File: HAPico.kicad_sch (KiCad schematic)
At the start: 30 parts, among them J1 GP 2, J2 GP 3, J3 GP 6, J4 GP 7, J5 GP10, J6 GP11, J7 GP20, J8 GP21, J9 Power Switch, Q1 IRLR024N, Q2 IRLR024N, Q3 IRLR024N, Q4 IRLR024N, Q5 IRLR024N, Q6 IRLR024N, Q7 IRLR024N, Q8 IRLR024N

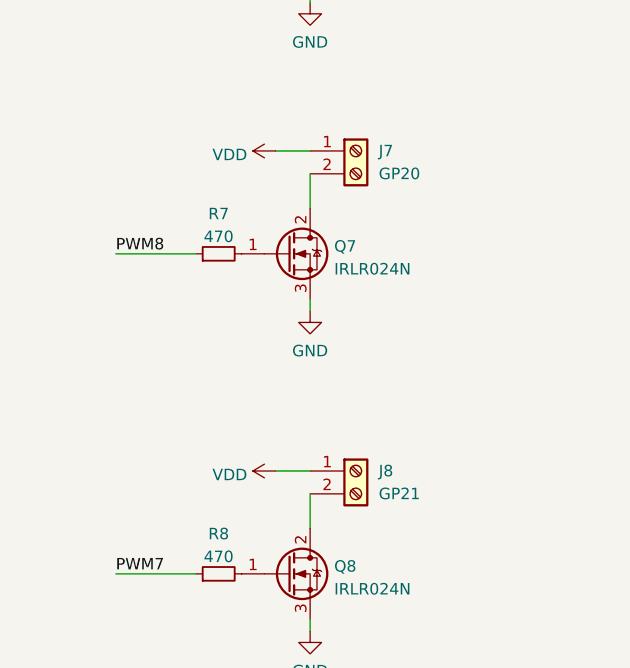
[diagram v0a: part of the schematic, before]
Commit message: fix: GP20 and 21 were swapped
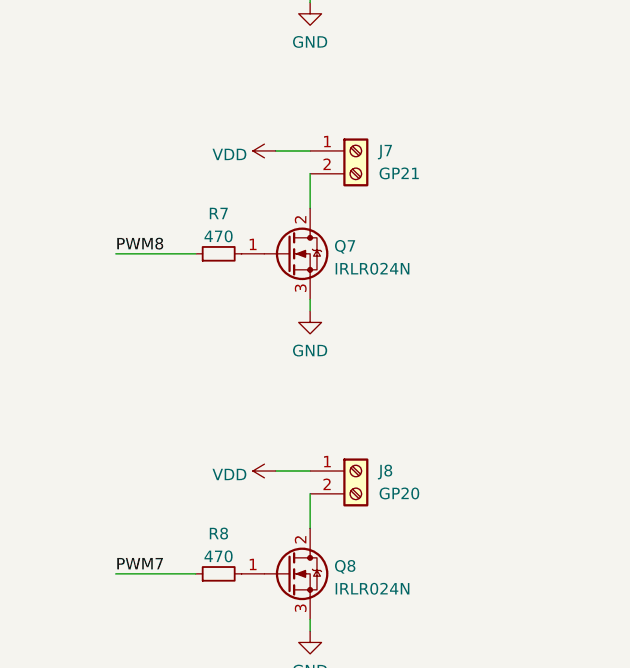
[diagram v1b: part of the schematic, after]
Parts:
- J7: value GP20 -> GP21
- J8: value GP21 -> GP20
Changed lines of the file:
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@@
 			)
 		)
-		(property "Value" "GP20"
+		(property "Value" "GP21"
 			(at 256.54 105.4099 0)
 			(effects
@@
 			)
 		)
-		(property "Value" "GP21"
+		(property "Value" "GP20"
 			(at 256.54 140.9699 0)
 			(effects
